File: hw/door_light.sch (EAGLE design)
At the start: 20 parts, among them IC1 TINY13-20PU, IC2 7805L, J1 PWR, J2 LIGHT, T1 2222a, T2 2222a, T3 LTR4602E

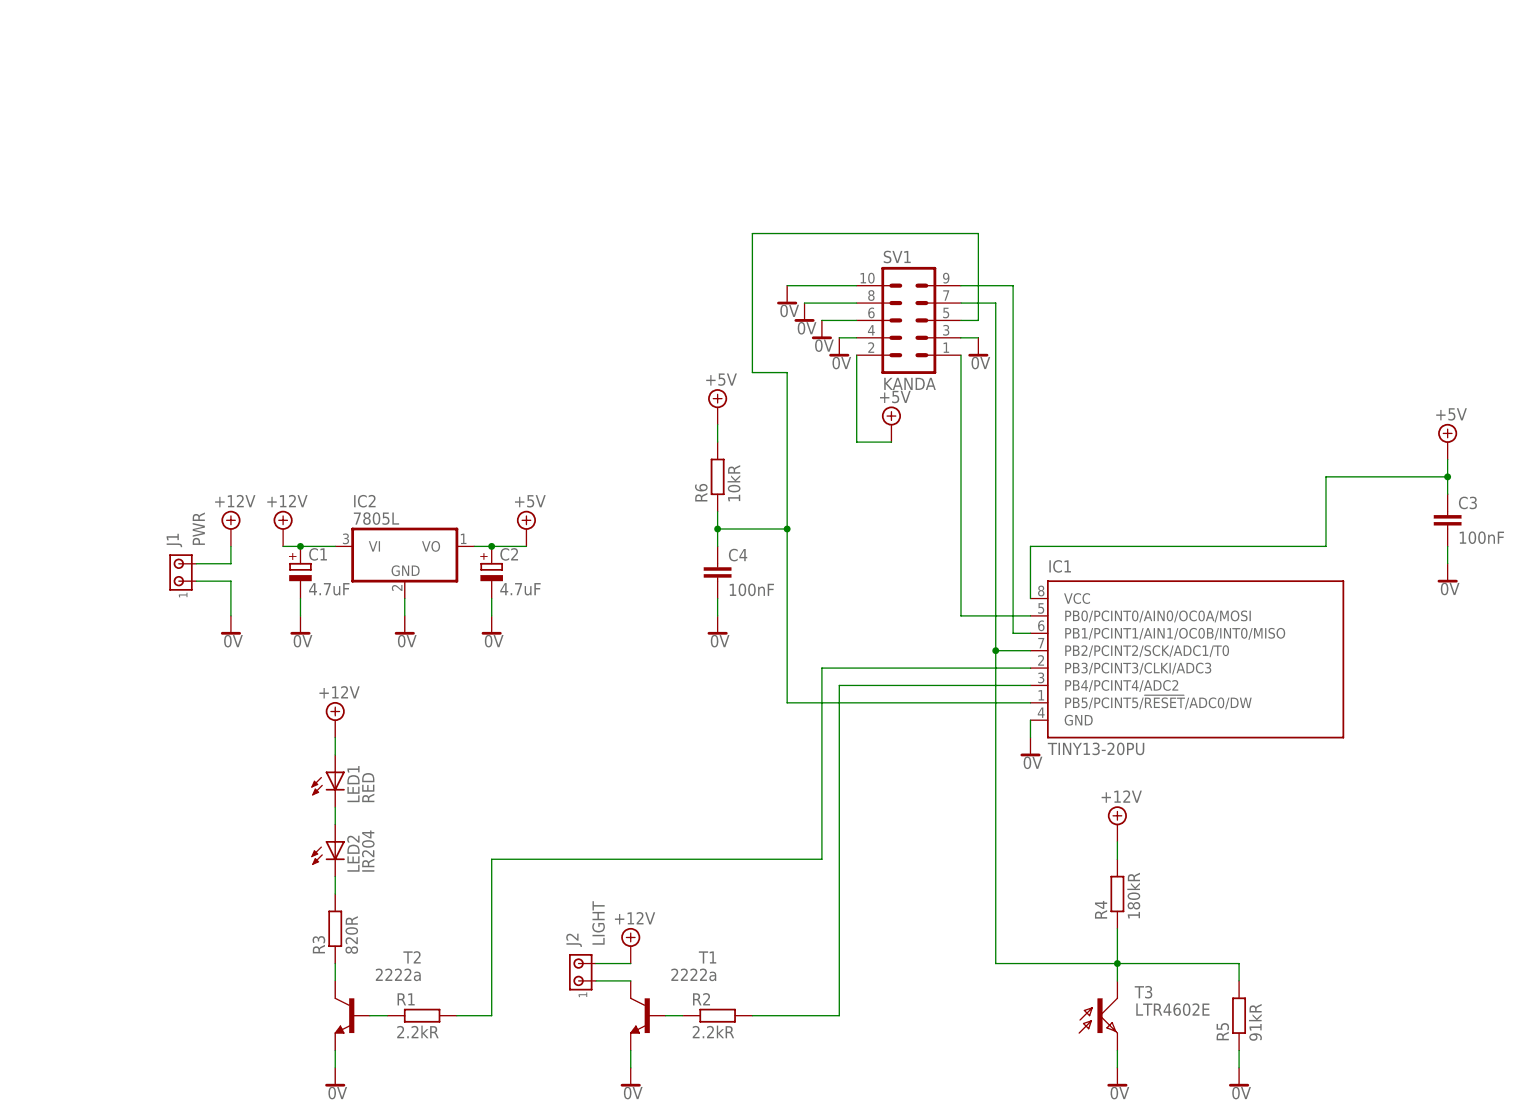
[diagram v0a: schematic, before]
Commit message: documentation update - now PCB is SMD
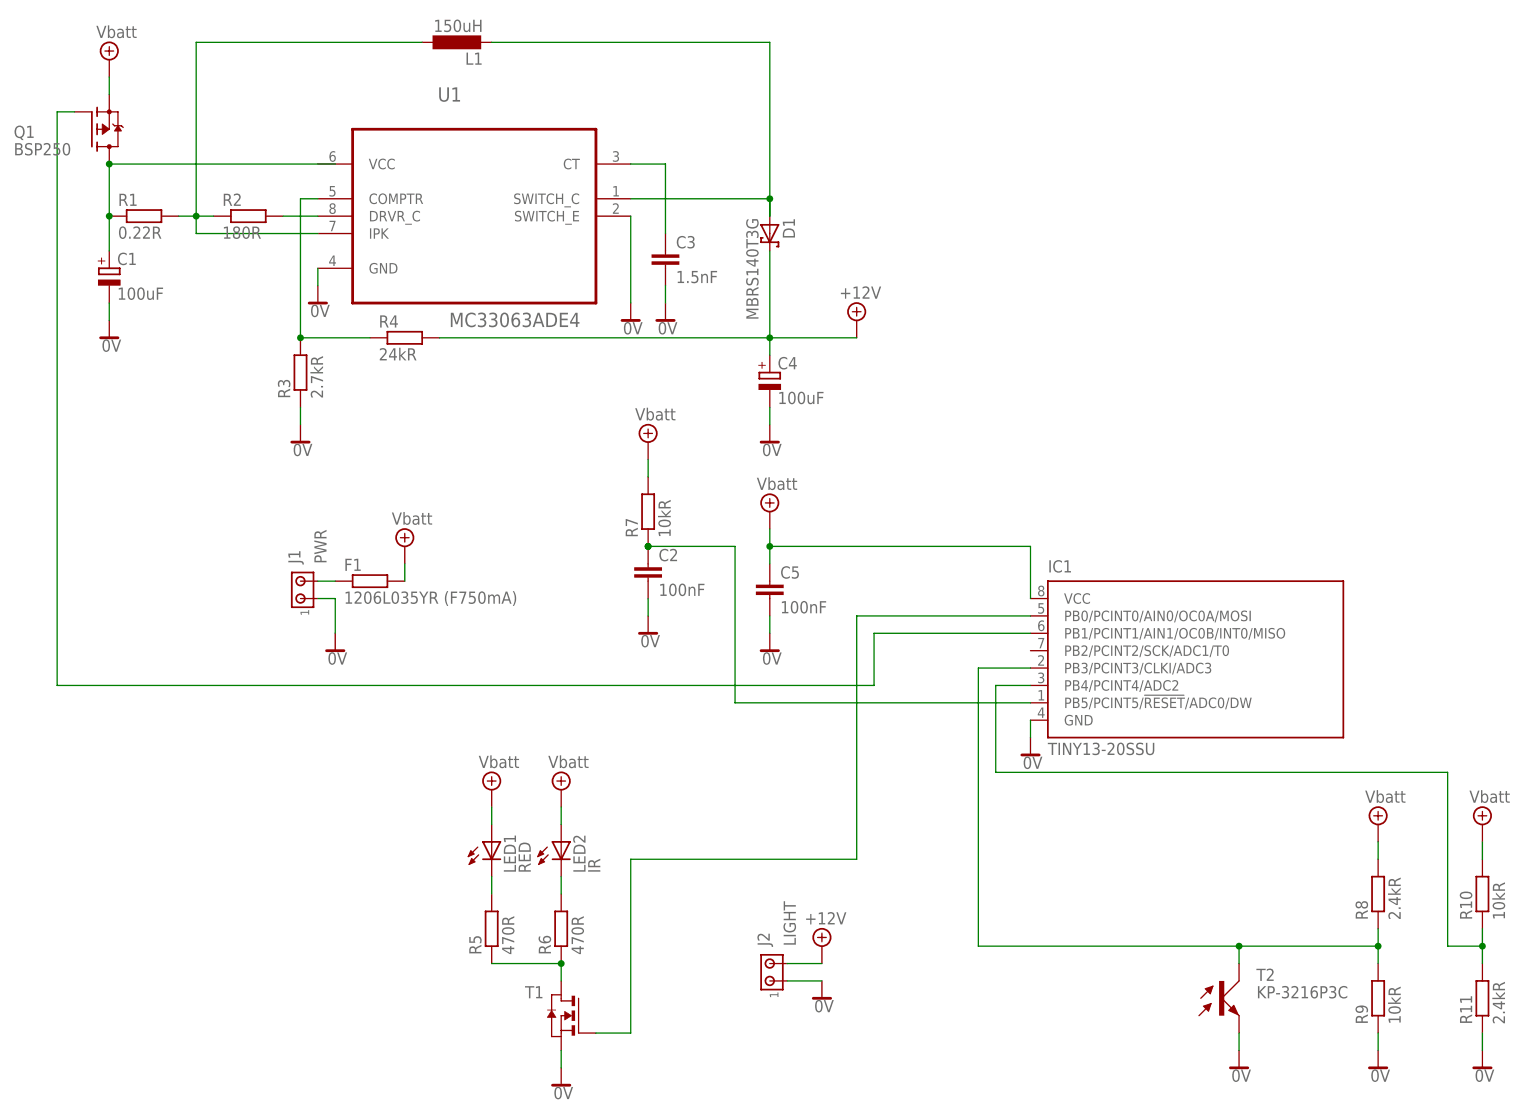
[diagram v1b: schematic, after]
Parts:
- removed IC2: 7805L, linear:7805L
- removed SV1: KANDA, con-harting-ml:ML10
- removed T3: LTR4602E, opto-trans-siemens:BPX81
- added C5: 100nF, rcl:C-EUC1206
- added D1: MBRS140T3G, diode:MBRS130LT3
- added F1: 1206L035YR (F750mA), rcl:R-EU_MELF0207W
- added L1: 150uH, rcl:L-EUL8530M
- added Q1: BSP250, transistor-fet:BSP170P
- added R10, R9: 10kR, rcl:R-EU_R0603
- added R11, R8: 2.4kR, rcl:R-EU_R0603
- added R7: 10kR, rcl:R-EU_R0402
- added U1: MC33063ADE4, Texas Instruments_By_element14_Batch_1:MC33063ADE4
- C1: value 4.7uF -> 100uF; device rcl:CPOL-EUE2,5-6E -> rcl:CPOL-EU153CLV-0810
- C2: value 4.7uF -> 100nF; device rcl:CPOL-EUE2,5-6E -> rcl:C-EUC1206
- C3: value 100nF -> 1.5nF; device rcl:C-EU025-025X050 -> rcl:C-EUC1206
- C4: value 100nF -> 100uF; device rcl:C-EU025-025X050 -> rcl:CPOL-EU153CLV-0810
- IC1: value TINY13-20PU -> TINY13-20SSU; device atmel:TINY13-20PU -> atmel:TINY13-20SSU
- LED1: device led:LED3MM -> led:LEDCHIPLED_0603
- LED2: value IR204 -> IR; device led:LED3MM -> led:LEDCHIPLED_0805
- R1: value 2.2kR -> 0.22R; device rcl:R-EU_0204/5 -> rcl:R-EU_R0603
- R2: value 2.2kR -> 180R; device rcl:R-EU_0204/5 -> rcl:R-EU_R0603
- R3: value 820R -> 2.7kR; device rcl:R-EU_0204/5 -> rcl:R-EU_R0603
- R4: value 180kR -> 24kR; device rcl:R-EU_0204/5 -> rcl:R-EU_R0603
- R5: value 91kR -> 470R; device rcl:R-EU_0204/5 -> rcl:R-EU_R0603
- R6: value 10kR -> 470R; device rcl:R-EU_0204/5 -> rcl:R-EU_R0603
- T1: value 2222a -> (none); device transistor-neu-to92:2N2222-NPN-TO92-EBC -> zetex:NMOSSOT23
- T2: value 2222a -> KP-3216P3C; device transistor-neu-to92:2N2222-NPN-TO92-EBC -> opto-trans-smd:KP-3216P3C
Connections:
- removed net +5V: C2.+, C3.1, IC1.VCC, IC2.VO, R6.2, SV1.2
- removed net N$5: J2.1, T1.C
- removed net N$6: R2.1, T1.B
- removed net N$7: IC1.PB2/PCINT2/SCK/ADC1/T0, R4.1, R5.2, SV1.7, T3.C
- new net +4.1V: C5.1, F1.2, IC1.VCC, LED1.A, LED2.A, Q1.S, R10.2, R7.2, R8.2
- new net N$10: C3.1, U1.CT
- new net N$11: D1.A, L1.2, U1.SWITCH_C
- new net N$15: R2.2, U1.DRVR_C
- new net N$16: L1.1, R1.2, R2.1, U1.IPK
- new net N$17: IC1.PB4/PCINT4/ADC2, R10.1, R11.2
- new net N$18: R3.2, R4.1, U1.COMPTR
- net +12V: now also C4.+, D1.C; no longer C1.+, IC2.VI, J1.2, LED1.A
- net 0V: now also C2.2, C4.-, C5.2, J2.1, R11.1, R3.1, R9.1, T1.S, U1.GND, U1.SWITCH_E; no longer C2.-, C4.2, IC2.GND, R5.1, SV1.10, SV1.3, SV1.4, SV1.6, SV1.8, T1.E, T3.E
- net N$1: now also R5.2; no longer LED2.A
- net N$12: now also IC1.PB3/PCINT3/CLKI/ADC3, R8.1, R9.2, T2.C; no longer IC1.PB1/PCINT1/AIN1/OC0B/INT0/MISO, SV1.9
- net N$13: now also IC1.PB1/PCINT1/AIN1/OC0B/INT0/MISO, Q1.G; no longer IC1.PB4/PCINT4/ADC2, R2.2
- net N$14: now also IC1.PB0/PCINT0/AIN0/OC0A/MOSI, T1.G; no longer IC1.PB3/PCINT3/CLKI/ADC3, R1.2
- net N$2: now also R6.2; no longer R3.2
- net N$3: now also C1.+, Q1.D; no longer T2.B
- net N$4: now also R5.1, R6.1, T1.D; no longer R3.1, T2.C
- net N$8: now also F1.1, J1.2; no longer IC1.PB0/PCINT0/AIN0/OC0A/MOSI, SV1.1
- net N$9: now also C2.1, R7.1; no longer C4.1, R6.1, SV1.5
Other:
- moved on the sheet: C1, C3, J1, J2, LED1, LED2, R1, R2, R3, R4, R5, R6

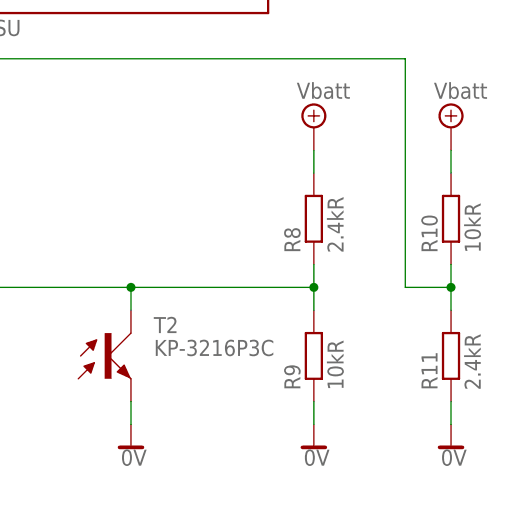
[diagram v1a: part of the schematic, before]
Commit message: fixed resistor voltage divider
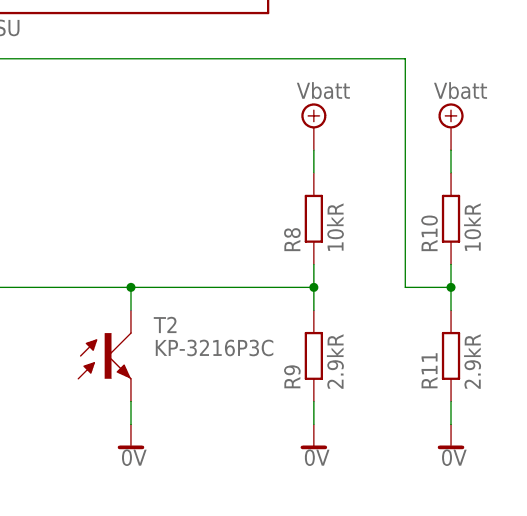
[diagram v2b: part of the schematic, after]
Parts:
- R11: value 2.4kR -> 2.9kR
- R8: value 2.4kR -> 10kR
- R9: value 10kR -> 2.9kR
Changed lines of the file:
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@@
 <part name="SUPPLY18" library="supply2" deviceset="+4.1V" device="" value="Vbatt"/>
 <part name="SUPPLY1" library="supply2" deviceset="+4.1V" device="" value="Vbatt"/>
-<part name="R9" library="rcl" deviceset="R-EU_" device="R0603" value="10kR"/>
+<part name="R9" library="rcl" deviceset="R-EU_" device="R0603" value="2.9kR"/>
 <part name="R10" library="rcl" deviceset="R-EU_" device="R0603" value="10kR"/>
-<part name="R8" library="rcl" deviceset="R-EU_" device="R0603" value="2.4kR"/>
-<part name="R11" library="rcl" deviceset="R-EU_" device="R0603" value="2.4kR"/>
+<part name="R8" library="rcl" deviceset="R-EU_" device="R0603" value="10kR"/>
+<part name="R11" library="rcl" deviceset="R-EU_" device="R0603" value="2.9kR"/>
 <part name="SUPPLY22" library="supply2" deviceset="+4.1V" device="" value="Vbatt"/>
 <part name="SUPPLY23" library="supply2" deviceset="+4.1V" device="" value="Vbatt"/>

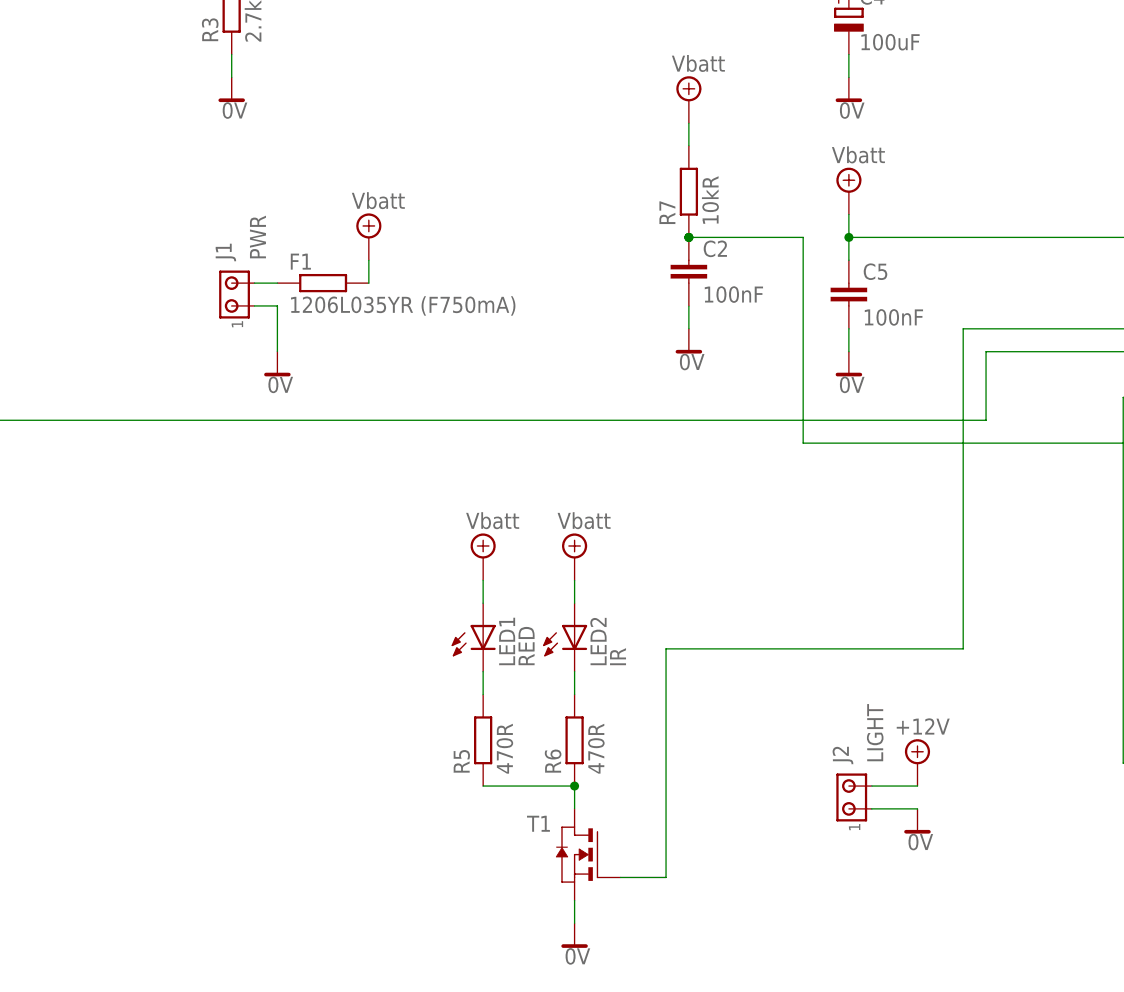
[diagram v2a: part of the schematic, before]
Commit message: pads for power and LED connecting are now SMD as well
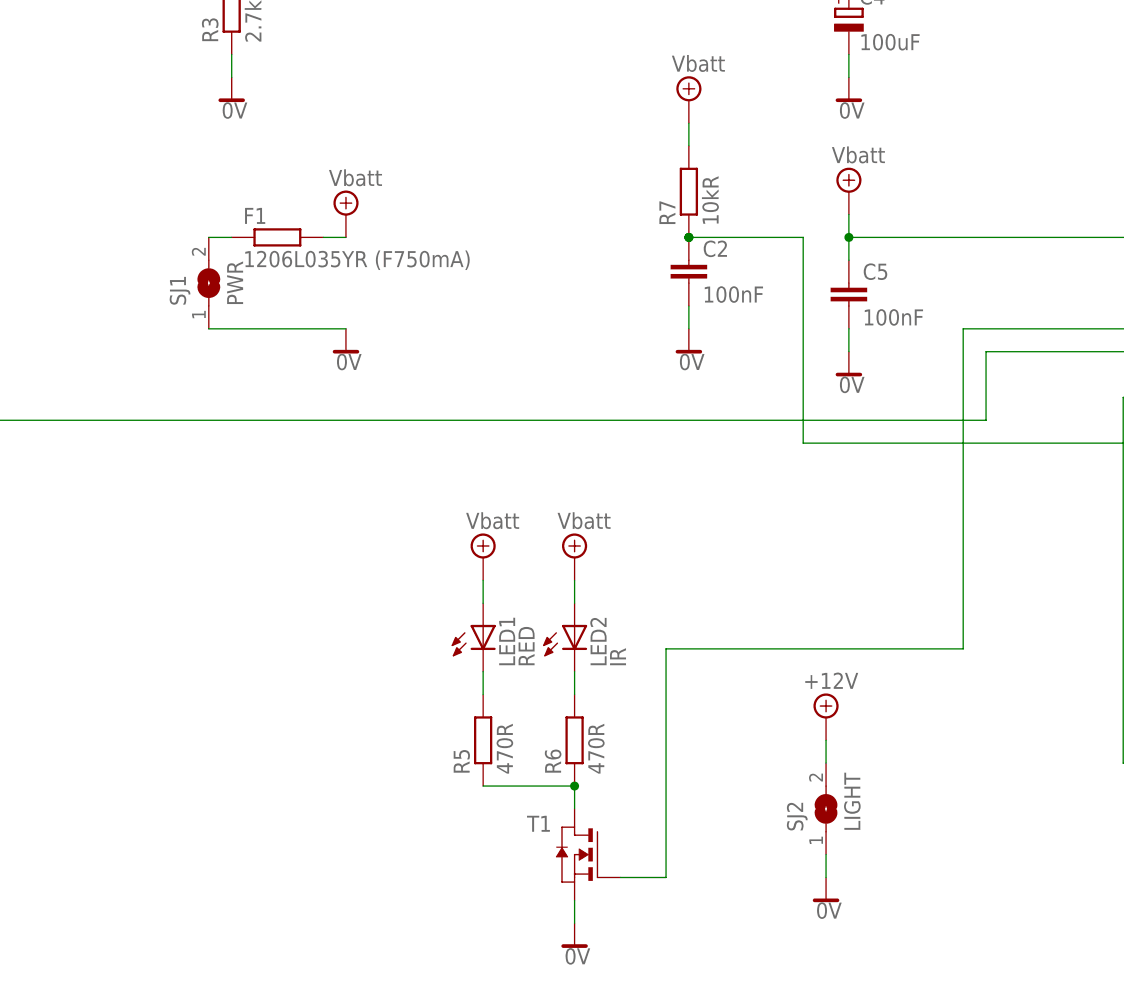
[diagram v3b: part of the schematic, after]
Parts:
- removed J1: PWR, con-amp:MTA02-100
- removed J2: LIGHT, con-amp:MTA02-100
- added SJ1: PWR, jumper:SJW
- added SJ2: LIGHT, jumper:SJW
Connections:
- net +12V: now also SJ2.2; no longer J2.2
- net 0V: now also SJ1.1, SJ2.1; no longer J1.1, J2.1
- net N$8: now also SJ1.2; no longer J1.2
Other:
- moved on the sheet: F1
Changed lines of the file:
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@@
 <part name="SUPPLY8" library="supply2" deviceset="0V" device=""/>
 <part name="SUPPLY10" library="supply2" deviceset="0V" device=""/>
-<part name="J1" library="con-amp" deviceset="MTA02-100" device="" value="PWR"/>
-<part name="J2" library="con-amp" deviceset="MTA02-100" device="" value="LIGHT"/>
 <part name="SUPPLY11" library="supply2" deviceset="+12V" device=""/>
 <part name="SUPPLY12" library="supply2" deviceset="0V" device=""/>
@@
 <part name="Q1" library="transistor-fet" deviceset="BSP170P" device="" value="BSP250"/>
 <part name="T1" library="zetex" deviceset="NMOSSOT23" device=""/>
+<part name="SJ1" library="jumper" deviceset="SJ" device="W" value="PWR"/>
+<part name="SJ2" library="jumper" deviceset="SJ" device="W" value="LIGHT"/>
 </parts>
 <sheets>
@@
 <instance part="SUPPLY8" gate="0V" x="60.96" y="68.58"/>
 <instance part="SUPPLY10" gate="0V" x="30.48" y="5.08"/>
-<instance part="J1" gate="G$1" x="-7.62" y="76.2" rot="R90"/>
-<instance part="J2" gate="G$1" x="60.96" y="20.32" rot="R90"/>
-<instance part="SUPPLY11" gate="+12V" x="68.58" y="25.4"/>
-<instance part="SUPPLY12" gate="0V" x="68.58" y="17.78"/>
-<instance part="SUPPLY14" gate="0V" x="-2.54" y="68.58"/>
+<instance part="SUPPLY11" gate="+12V" x="58.42" y="30.48"/>
+<instance part="SUPPLY12" gate="0V" x="58.42" y="10.16"/>
+<instance part="SUPPLY14" gate="0V" x="5.08" y="71.12"/>
 <instance part="C2" gate="G$1" x="43.18" y="81.28"/>
 <instance part="SUPPLY19" gate="0V" x="43.18" y="71.12"/>
 <instance part="U1" gate="A" x="17.78" y="134.62"/>
-<instance part="SUPPLY26" gate="P" x="7.62" y="83.82"/>
-<instance part="F1" gate="G$1" x="2.54" y="78.74"/>
+<instance part="SUPPLY26" gate="P" x="5.08" y="86.36"/>
+<instance part="F1" gate="G$1" x="-2.54" y="83.82"/>
 <instance part="R7" gate="G$1" x="43.18" y="88.9" rot="R90"/>
 <instance part="D1" gate="G$1" x="60.96" y="129.54" rot="R270"/>
@@
 <instance part="Q1" gate="G$1" x="-38.1" y="144.78"/>
 <instance part="T1" gate="A" x="30.48" y="15.24" rot="MR0"/>
+<instance part="SJ1" gate="1" x="-10.16" y="78.74" rot="R90"/>
+<instance part="SJ2" gate="1" x="58.42" y="20.32" rot="R90"/>
 </instances>
 <busses>
@@
 </segment>
 <segment>
-<pinref part="J1" gate="G$1" pin="1"/>
-<pinref part="SUPPLY14" gate="0V" pin="0V"/>
-<wire x1="-2.54" y1="71.12" x2="-2.54" y2="76.2" width="0.1524" layer="91"/>
-<wire x1="-2.54" y1="76.2" x2="-5.08" y2="76.2" width="0.1524" layer="91"/>
-</segment>
-<segment>
 <pinref part="C2" gate="G$1" pin="2"/>
 <pinref part="SUPPLY19" gate="0V" pin="0V"/>
@@
 </segment>
 <segment>
-<pinref part="J2" gate="G$1" pin="1"/>
+<pinref part="SJ2" gate="1" pin="1"/>
 <pinref part="SUPPLY12" gate="0V" pin="0V"/>
-<wire x1="68.58" y1="20.32" x2="63.5" y2="20.32" width="0.1524" layer="91"/>
+<wire x1="58.42" y1="12.7" x2="58.42" y2="15.24" width="0.1524" layer="91"/>
+</segment>
+<segment>
+<pinref part="SJ1" gate="1" pin="1"/>
+<pinref part="SUPPLY14" gate="0V" pin="0V"/>
+<wire x1="5.08" y1="73.66" x2="-10.16" y2="73.66" width="0.1524" layer="91"/>
 </segment>
 </net>
 <net name="+12V" class="0">
-<segment>
-<pinref part="J2" gate="G$1" pin="2"/>
-<pinref part="SUPPLY11" gate="+12V" pin="+12V"/>
-<wire x1="68.58" y1="22.86" x2="63.5" y2="22.86" width="0.1524" layer="91"/>
-</segment>
 <segment>
 <pinref part="D1" gate="G$1" pin="C"/>
@@
 <pinref part="R4" gate="G$1" pin="2"/>
 </segment>
+<segment>
+<pinref part="SJ2" gate="1" pin="2"/>
+<pinref part="SUPPLY11" gate="+12V" pin="+12V"/>
+<wire x1="58.42" y1="27.94" x2="58.42" y2="25.4" width="0.1524" layer="91"/>
+</segment>
 </net>
 <net name="N$2" class="0">
@@
 <net name="+4.1V" class="0">
 <segment>
-<wire x1="7.62" y1="81.28" x2="7.62" y2="78.74" width="0.1524" layer="91"/>
+<wire x1="5.08" y1="83.82" x2="2.54" y2="83.82" width="0.1524" layer="91"/>
 <pinref part="SUPPLY26" gate="P" pin="+4.1V"/>
 <pinref part="F1" gate="G$1" pin="2"/>
@@
 <net name="N$8" class="0">
 <segment>
-<pinref part="J1" gate="G$1" pin="2"/>
 <pinref part="F1" gate="G$1" pin="1"/>
-<wire x1="-2.54" y1="78.74" x2="-5.08" y2="78.74" width="0.1524" layer="91"/>
-</segment>
-</net>
+<wire x1="-7.62" y1="83.82" x2="-10.16" y2="83.82" width="0.1524" layer="91"/>
+<pinref part="SJ1" gate="1" pin="2"/>
+</segment>
+</net>

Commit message: coil type changed (bigger one)
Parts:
- L1: device rcl:L-EUL8530M -> rcl:L-EUPIS2816
- R2: device rcl:R-EU_R0603 -> rcl:R-EU_M1206
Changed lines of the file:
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@@
 <part name="C1" library="rcl" deviceset="CPOL-EU" device="153CLV-0810" value="100uF"/>
 <part name="C4" library="rcl" deviceset="CPOL-EU" device="153CLV-0810" value="100uF"/>
-<part name="L1" library="rcl" deviceset="L-EU" device="L8530M" value="150uH"/>
-<part name="R2" library="rcl" deviceset="R-EU_" device="R0603" value="180R"/>
+<part name="L1" library="rcl" deviceset="L-EU" device="PIS2816" value="150uH"/>
+<part name="R2" library="rcl" deviceset="R-EU_" device="M1206" value="180R"/>
 <part name="R1" library="rcl" deviceset="R-EU_" device="R0603" value="0.22R"/>
 <part name="SUPPLY13" library="supply2" deviceset="0V" device=""/>
